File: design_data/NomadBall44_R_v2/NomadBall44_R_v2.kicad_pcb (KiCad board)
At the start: 2 copper layers, 147.4 x 96.5 mm, 57 parts, among them SW1 SW_Push, SW10 SW_Push, SW11 SW_Push, SW12 SW_Push, SW13 SW_Push, SW14 SW_Push, SW15 SW_Push, SW16 SW_Push, SW17 SW_Push, SW18 SW_Push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

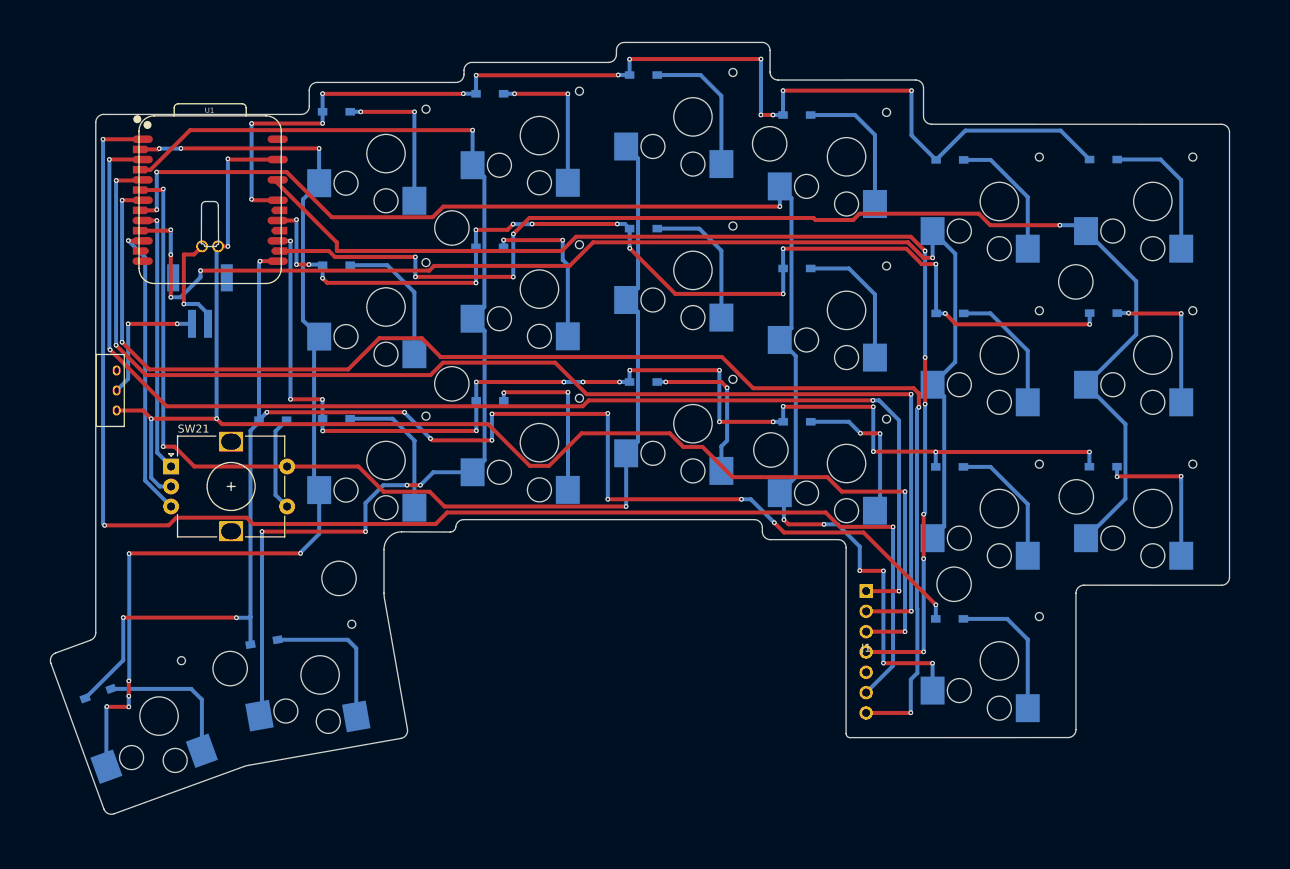
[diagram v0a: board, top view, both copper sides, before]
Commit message: ノイズ対策でGNDで塗りつぶし
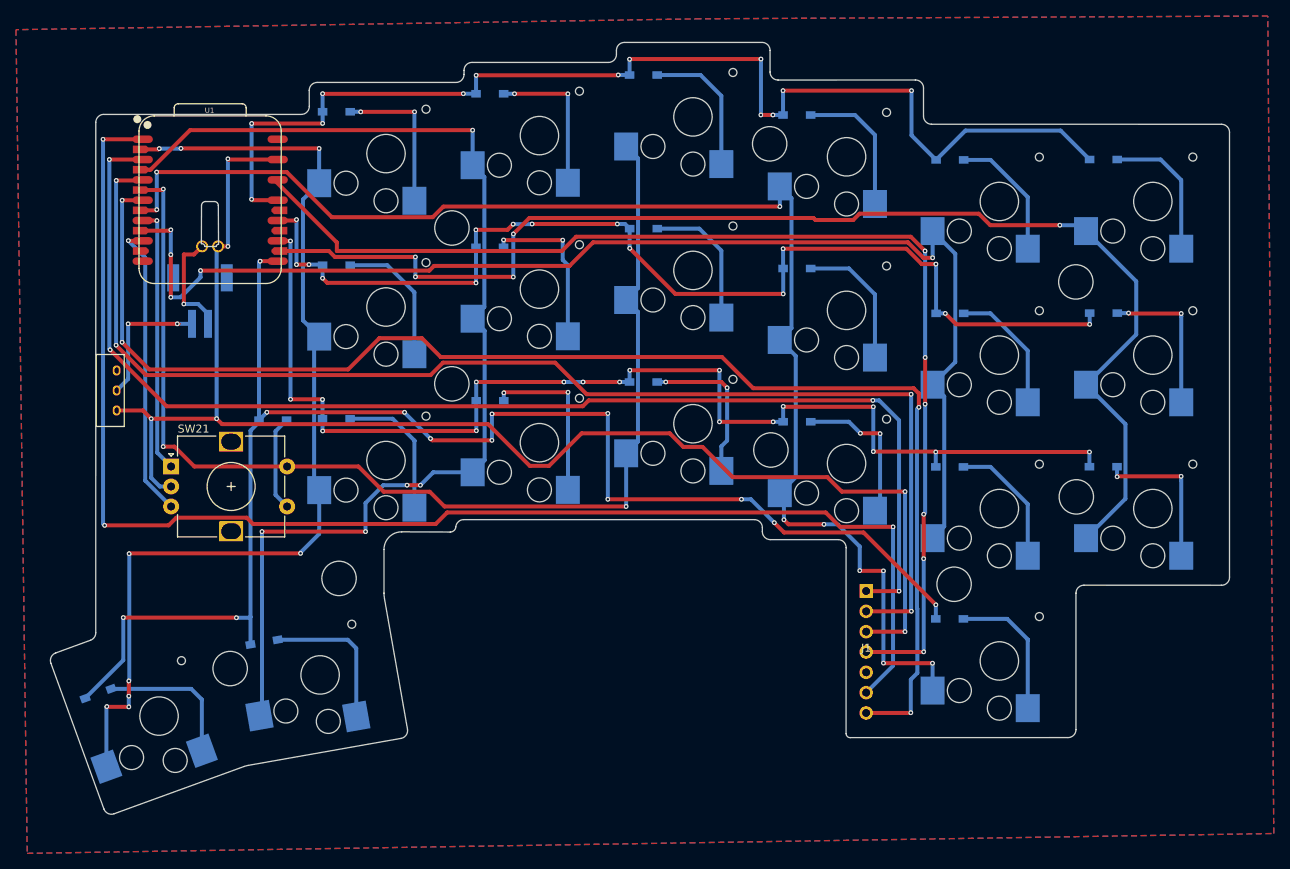
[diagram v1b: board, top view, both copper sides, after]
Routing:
- added copper zone on B.Cu, net GND
- added copper zone on F.Cu, net GND
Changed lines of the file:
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@@
 		(net 43)
+	)
+	(zone
+		(net 32)
+		(net_name "GND")
+		(layers "F.Cu" "B.Cu")
+		(hatch edge 0.5)
+		(connect_pads
+			(clearance 0.5)
+		)
+		(min_thickness 0.25)
+		(filled_areas_thickness no)
+		(fill yes
+			(thermal_gap 0.5)
+			(thermal_bridge_width 0.5)
+			(island_removal_mode 1)
+			(island_area_min 10)
+		)
+		(polygon
+			(pts
+				(xy 154.54 37.76) (xy 69 39.12) (xy 70.4 142.08) (xy 226.22 139.6) (xy 225.48 37.41)
+			)
+		)
 	)
 	(embedded_fonts no)
